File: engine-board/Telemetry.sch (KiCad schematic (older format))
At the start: 5 parts, among them J501 Serial Telemetry, J502 NEO08MU GPS, J503 RockBLOCK 9603, J504 RockBlock9603, U501 RockBLOCK 9603 Accessory Cable

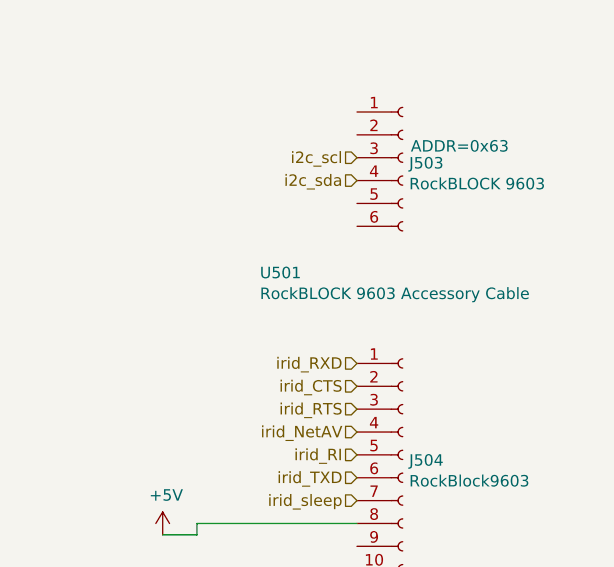
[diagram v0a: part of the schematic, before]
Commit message: pcb parts done, footprints updated, ready for routing
pre-routing step..
- finalized footprints
- verified layout, size, mounting holes (1.75" apart)
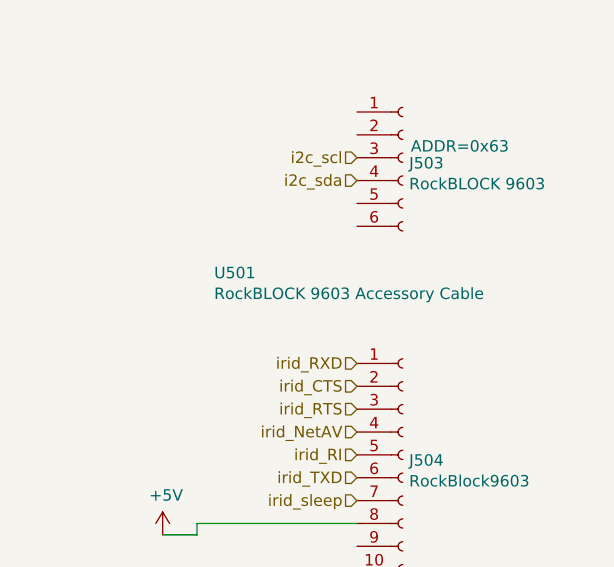
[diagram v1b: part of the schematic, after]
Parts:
- J504: footprint (none) -> Connector_PinSocket_2.54mm:PinSocket_1x10_P2.54mm_Vertical
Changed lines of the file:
@@
 L Device:HW U501
 U 1 1 61AFA4DA
-P 8400 3100
-F 0 "U501" H 8425 3146 50  0000 L CNN
-F 1 "RockBLOCK 9603 Accessory Cable" H 8425 3055 50  0000 L CNN
-F 2 "" H 8400 3100 50  0001 C CNN
-F 3 "" H 8400 3100 50  0001 C CNN
-F 4 "4.95" H 8400 3100 50  0001 C CNN "Price"
-F 5 "4529" H 8400 3100 50  0001 C CNN "MPM"
-F 6 "https://www.adafruit.com/product/4529" H 8400 3100 50  0001 C CNN "Link"
-	1    8400 3100
+P 8200 3100
+F 0 "U501" H 8225 3146 50  0000 L CNN
+F 1 "RockBLOCK 9603 Accessory Cable" H 8225 3055 50  0000 L CNN
+F 2 "" H 8200 3100 50  0001 C CNN
+F 3 "" H 8200 3100 50  0001 C CNN
+F 4 "4.95" H 8200 3100 50  0001 C CNN "Price"
+F 5 "4529" H 8200 3100 50  0001 C CNN "MPM"
+F 6 "https://www.adafruit.com/product/4529" H 8200 3100 50  0001 C CNN "Link"
+	1    8200 3100
 	1    0    0    -1
 $EndComp
@@
 F 0 "J504" H 9078 3826 50  0000 L CNN
 F 1 "RockBlock9603" H 9078 3735 50  0000 L CNN
-F 2 "" H 9050 3850 50  0001 C CNN
+F 2 "Connector_PinSocket_2.54mm:PinSocket_1x10_P2.54mm_Vertical" H 9050 3850 50  0001 C CNN
 F 3 "~" H 9050 3850 50  0001 C CNN
 	1    9050 3850

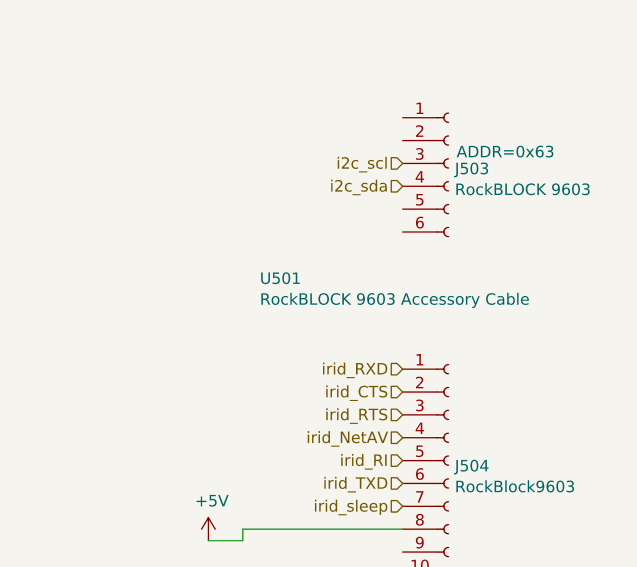
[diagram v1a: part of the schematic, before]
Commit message: shortend pcb, ready to route
ready to route, shortend pcb, layout complete
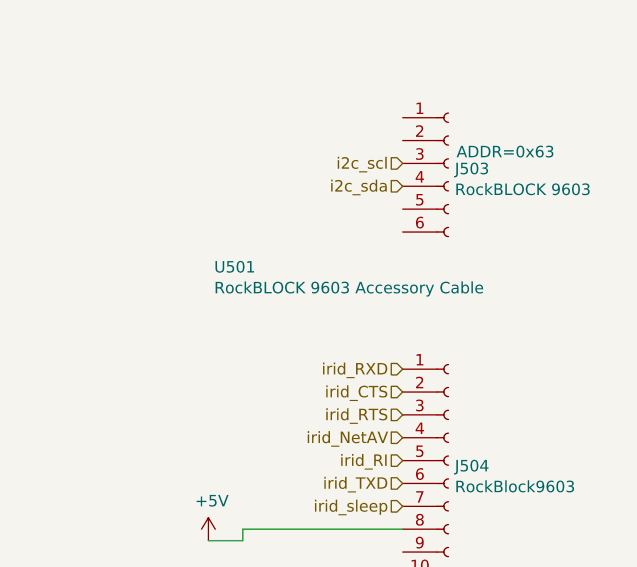
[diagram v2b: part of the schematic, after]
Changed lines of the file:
@@
 L Device:HW U501
 U 1 1 61AFA4DA
-P 8200 3100
-F 0 "U501" H 8225 3146 50  0000 L CNN
-F 1 "RockBLOCK 9603 Accessory Cable" H 8225 3055 50  0000 L CNN
-F 2 "" H 8200 3100 50  0001 C CNN
-F 3 "" H 8200 3100 50  0001 C CNN
-F 4 "4.95" H 8200 3100 50  0001 C CNN "Price"
-F 5 "4529" H 8200 3100 50  0001 C CNN "MPM"
-F 6 "https://www.adafruit.com/product/4529" H 8200 3100 50  0001 C CNN "Link"
-	1    8200 3100
+P 8000 3050
+F 0 "U501" H 8025 3096 50  0000 L CNN
+F 1 "RockBLOCK 9603 Accessory Cable" H 8025 3005 50  0000 L CNN
+F 2 "" H 8000 3050 50  0001 C CNN
+F 3 "" H 8000 3050 50  0001 C CNN
+F 4 "4.95" H 8000 3050 50  0001 C CNN "Price"
+F 5 "4529" H 8000 3050 50  0001 C CNN "MPM"
+F 6 "https://www.adafruit.com/product/4529" H 8000 3050 50  0001 C CNN "Link"
+	1    8000 3050
 	1    0    0    -1
 $EndComp

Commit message: Verions 1.0 done + ordered
added routes, submitted order
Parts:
- removed J501: Serial Telemetry, TerminalBlock_CUI:CUI_TBP01R1W-508-04BE, symbol Connector_Generic:Conn_02x02_Top_Bottom
- J502, J503: Price2 (none) -> 0
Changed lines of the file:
@@
 Wire Wire Line
 	7950 1300 8800 1300
-$Comp
-L power:+5V #PWR0502
-U 1 1 6190BE9A
-P 4750 1200
-F 0 "#PWR0502" H 4750 1050 50  0001 C CNN
-F 1 "+5V" H 4765 1373 50  0000 C CNN
-F 2 "" H 4750 1200 50  0001 C CNN
-F 3 "" H 4750 1200 50  0001 C CNN
-	1    4750 1200
-	1    0    0    -1
-$EndComp
-$Comp
-L power:GND #PWR0501
-U 1 1 6190BEA0
-P 4500 1300
-F 0 "#PWR0501" H 4500 1050 50  0001 C CNN
-F 1 "GND" H 4505 1127 50  0000 C CNN
-F 2 "" H 4500 1300 50  0001 C CNN
-F 3 "" H 4500 1300 50  0001 C CNN
-	1    4500 1300
-	1    0    0    -1
-$EndComp
-$Comp
-L Connector_Generic:Conn_02x02_Top_Bottom J501
-U 1 1 6190BEAA
-P 5400 1200
-F 0 "J501" H 5450 1417 50  0000 C CNN
-F 1 "Serial Telemetry" H 5450 1326 50  0000 C CNN
-F 2 "TerminalBlock_CUI:CUI_TBP01R1W-508-04BE" H 5400 1200 50  0001 C CNN
-F 3 "~" H 5400 1200 50  0001 C CNN
-F 4 "https://www.digikey.com/en/products/detail/cui-devices/TBP01R1W-508-04BE/10238427?WT.z_cid=ref_neda_dkc_buynow_cuidevices&utm_source=ecia&utm_medium=aggregator&utm_campaign=cuidevices" H 5400 1200 50  0001 C CNN "Link"
-F 5 "CUI Devices" H 5400 1200 50  0001 C CNN "MANUFACTURER"
-F 6 "TBP01R1W-508-04BE" H 5400 1200 50  0001 C CNN "MPN"
-F 7 "1.28" H 5400 1200 50  0001 C CNN "Price"
-	1    5400 1200
-	1    0    0    -1
-$EndComp
-Wire Wire Line
-	4750 1200 5200 1200
-Wire Wire Line
-	4500 1300 5200 1300
-Text HLabel 5700 1200 2    50   Input ~ 0
-usb_data_D0
-Text HLabel 5700 1300 2    50   Input ~ 0
-usb_data_D1
 Text HLabel 7950 1000 0    50   Input ~ 0
 gps_pps
@@
 F 7 "249.95" H 9050 2550 50  0001 C CNN "Price"
 F 8 "ADDR=0x63" H 9300 2600 50  0000 C CNN "I2C_ADDR"
+F 9 "0" H 9050 2550 50  0001 C CNN "Price2"
 	1    9050 2550
 	1    0    0    -1
@@
 F 7 "1.68" H 9000 1300 50  0001 C CNN "Price"
 F 8 "ADDR=0x42" H 9250 1350 50  0000 C CNN "I2C_ADDR"
+F 9 "0" H 9000 1300 50  0001 C CNN "Price2"
 	1    9000 1300
 	1    0    0    -1

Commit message: board smaller
PCB V0.1 Errata:

- [QUESTION: - it looks like 12 on website] polulu 2814 has 16 pin footprint instead of 12...  AAACK!!!
- 5v and 3.3v traces could be wider
- [FIXED] fail: going into the power schematic scl + sda are swapped...
- [FIXED - moved to miniofit] pump controller silkscreen is wrong
- [FIXED] NOTE: just switch ALL to the minifit??
- [FIXED - will be on top, but not needed now] ADD: Ethernet connection from the teensy to the host computer board.
- [FIXED - going to use Qwiic) 9 Axis Mopak: wrong footprint - holes too small, spacing seems good, create outline as it bumps into feather header
- [FIXED] RV1805:  power + GND swapped... and I can’t seem to find them.
- [FIXED] 2 pressure sensors, the same i2c address... rerouted to 2nd i2c port on teensy
- [NOT NEEDED - adding display] Add RGB LED... it will be helpful for debugging.
- [FIXED - kindof - moved to micro-fit, might need to wire this directly to bulkhead] Turbine ferrules for power are 12 gauge - need bigger screw terminals if that is the connection method
- [FIXED] Feather footprint - lookup exactly what feather boards need for support..
- [FIXED] pump_motor_pwm is not connected to the TEENSY!!  blerg.  (jumper to pin 13 of feather for now)
- [FIXED - added FET] Maxon 70/30 POWER?  Think about power FET or ‘sleep’ to turn it off.
- [FIXED - added to bulkhead connector] Teensy 4.1 Program + ON/OFF pins - research how to extend these
- [TODO] remove VL6180 range sensor
- [LATER - will add to cost.. possibly remove?] put battery on back side
- add silkscreen for polulu
- [FIXED] Reorganize connectors:
    - Pump motor connectors go on end - attached in closing
    - bulkhead connectors go on side as they will always be attached
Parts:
- J502: Link2 (none) -> https://www.sparkfun.com/products/16329; MANUFACTURER Samtec Inc. -> (none); MATE_Link (none) -> https://www.digikey.com/en/products/detail/molex/0901210128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; MATE_MPN (none) -> 0901210128; MATE_Price (none) -> 1.16; Manufacturer (none) -> Sparkfun; Price2 0 -> 74.95
- J503: Link https://www.adafruit.com/product/4521 -> https://www.digikey.com/en/products/detail/samtec-inc/SSQ-1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; Link2 (none) -> https://www.adafruit.com/product/4521; MANUFACTURER Adafruit -> (none); Manufacturer (none) -> Adafruit; Price 249.95 -> 2.10; Price2 0 -> 249.95
- U501: MPM 4529 -> (none); MPN (none) -> 4529
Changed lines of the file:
@@
 F 2 "Connector_PinSocket_2.54mm:PinSocket_1x10_P2.54mm_Vertical" H 9050 2550 50  0001 C CNN
 F 3 "~" H 9050 2550 50  0001 C CNN
-F 4 "https://www.adafruit.com/product/4521" H 9050 2550 50  0001 C CNN "Link"
-F 5 "Adafruit" H 9050 2550 50  0001 C CNN "MANUFACTURER"
+F 4 "https://www.digikey.com/en/products/detail/samtec-inc/SSQ-110-01-G-S/1110609" H 9050 2550 50  0001 C CNN "Link"
+F 5 "" H 9050 2550 50  0001 C CNN "MANUFACTURER"
 F 6 "RockBLOCK 9603" H 9050 2550 50  0001 C CNN "MPN"
-F 7 "249.95" H 9050 2550 50  0001 C CNN "Price"
+F 7 "2.10" H 9050 2550 50  0001 C CNN "Price"
 F 8 "ADDR=0x63" H 9300 2600 50  0000 C CNN "I2C_ADDR"
-F 9 "0" H 9050 2550 50  0001 C CNN "Price2"
+F 9 "249.95" H 9050 2550 50  0001 C CNN "Price2"
+F 10 "https://www.adafruit.com/product/4521" H 9050 2550 50  0001 C CNN "Link2"
+F 11 "Adafruit" H 9050 2550 50  0001 C CNN "Manufacturer"
 	1    9050 2550
 	1    0    0    -1
@@
 F 3 "" H 8000 3050 50  0001 C CNN
 F 4 "4.95" H 8000 3050 50  0001 C CNN "Price"
-F 5 "4529" H 8000 3050 50  0001 C CNN "MPM"
+F 5 "" H 8000 3050 50  0001 C CNN "MPM"
 F 6 "https://www.adafruit.com/product/4529" H 8000 3050 50  0001 C CNN "Link"
+F 7 "4529" H 8000 3050 50  0001 C CNN "MPN"
 	1    8000 3050
 	1    0    0    -1
@@
 F 3 "~" H 9000 1300 50  0001 C CNN
 F 4 "https://www.digikey.com/en/products/detail/samtec-inc/SSQ-108-01-G-S/1110611" H 9000 1300 50  0001 C CNN "Link"
-F 5 "Samtec Inc." H 9000 1300 50  0001 C CNN "MANUFACTURER"
+F 5 "" H 9000 1300 50  0001 C CNN "MANUFACTURER"
 F 6 "SSQ-108-01-G-S" H 9000 1300 50  0001 C CNN "MPN"
 F 7 "1.68" H 9000 1300 50  0001 C CNN "Price"
 F 8 "ADDR=0x42" H 9250 1350 50  0000 C CNN "I2C_ADDR"
-F 9 "0" H 9000 1300 50  0001 C CNN "Price2"
+F 9 "74.95" H 9000 1300 50  0001 C CNN "Price2"
+F 10 "https://www.sparkfun.com/products/16329" H 9000 1300 50  0001 C CNN "Link2"
+F 11 "https://www.digikey.com/en/products/detail/molex/0901210128/760817?s=N4IgTCBcDaIJwAYCMYnLADhAXQL5A" H 9000 1300 50  0001 C CNN "MATE_Link"
+F 12 "0901210128" H 9000 1300 50  0001 C CNN "MATE_MPN"
+F 13 "1.16" H 9000 1300 50  0001 C CNN "MATE_Price"
+F 14 "Sparkfun" H 9000 1300 50  0001 C CNN "Manufacturer"
 	1    9000 1300
 	1    0    0    -1
